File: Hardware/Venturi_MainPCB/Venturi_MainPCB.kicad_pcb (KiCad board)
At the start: 2 copper layers, 166.1 x 84.5 mm, 75 parts, among them J1 Battery, J2 ESC_PWM, J3 ESC_P, J4 ESC_N, J5 M1, J6 M1, J7 Sensor-PCB, Q1 BSS138, Q2 DMP3013SFV, U1 TSOP38238, U2 ESP32-P4-WIFI6, U3 MIC29152WU, U4 DRV8212P, U5 DRV8212P, U6 ICM-20948

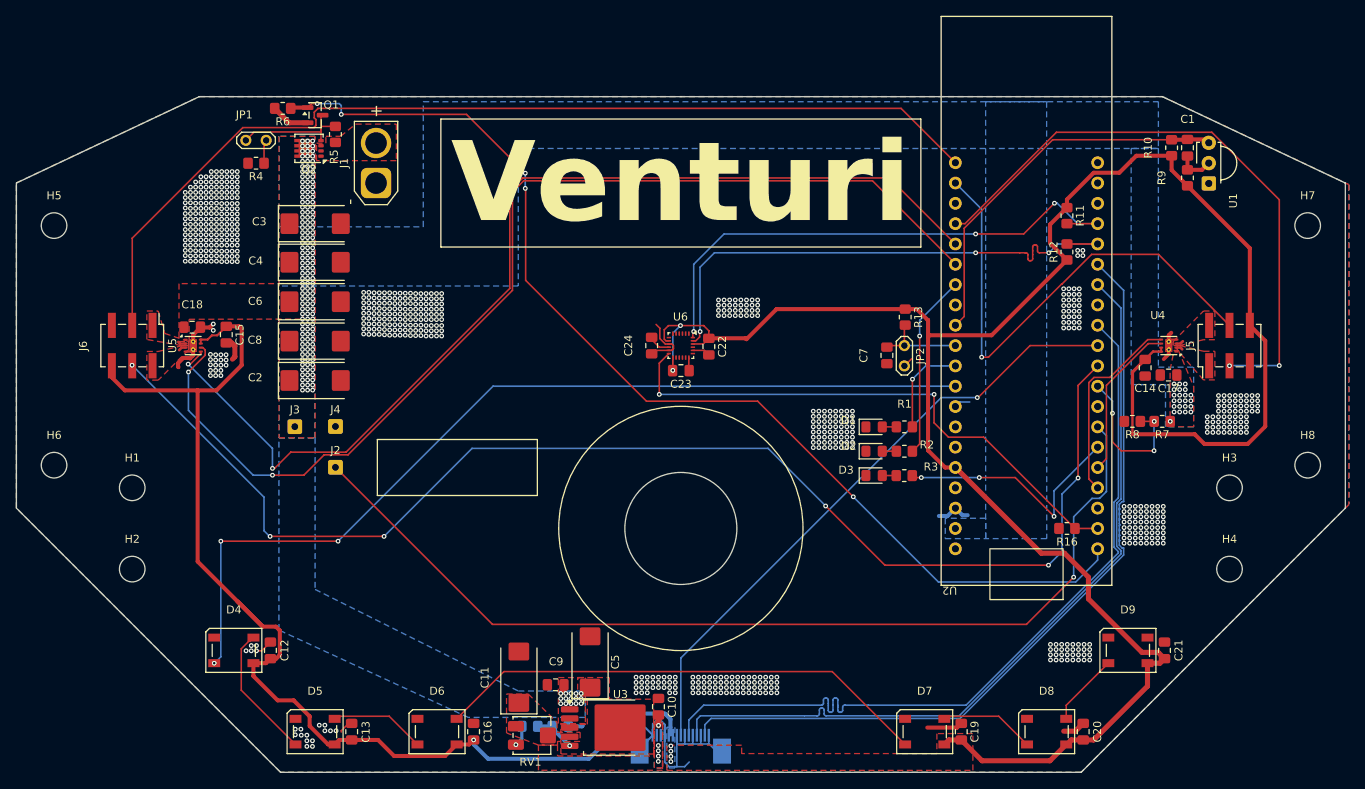
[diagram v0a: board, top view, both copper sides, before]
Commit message: Updated PCB-Design for 20MHz SPI speed
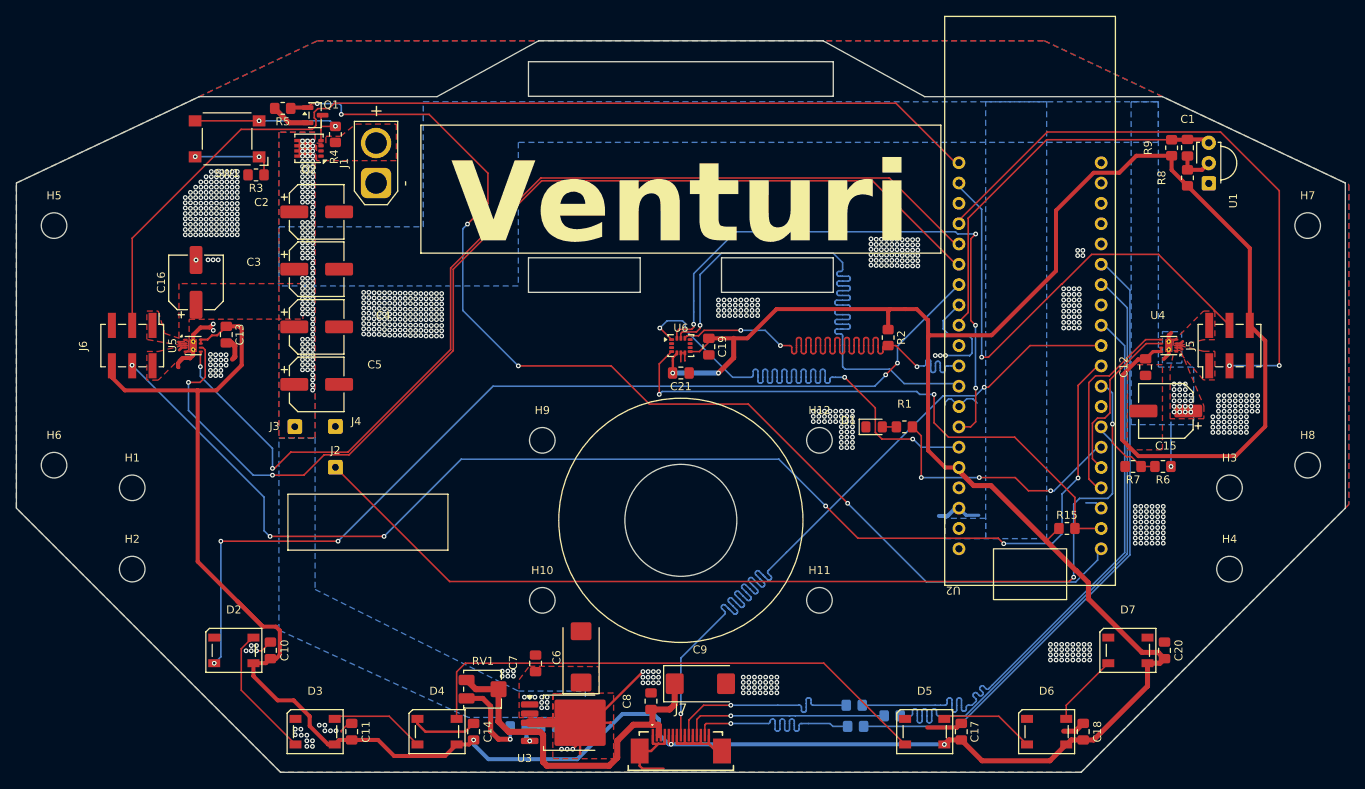
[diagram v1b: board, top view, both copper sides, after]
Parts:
- removed the C17 at (198.8, 93.0)
- removed the C18 at (76.8, 87.0)
- removed C24: 100n, Capacitor_SMD:C_0805_2012Metric_Pad1.18x1.45mm_HandSolder
- removed the C6 at (92.1, 83.8)
- removed the C7 at (163.6, 90.5)
- removed the C8 at (92.1, 88.7)
- removed the D2 at (162.0, 102.5)
- removed the D3 at (162.0, 105.5)
- removed JP1: POWER_EN, TestPoint:TestPoint_2Pads_Pitch2.54mm_Drill0.8mm
- removed JP2: ESP_EN, TestPoint:TestPoint_2Pads_Pitch2.54mm_Drill0.8mm
- removed the R13 at (165.9, 85.7)
- removed the R2 at (165.8, 102.5)
- removed the R3 at (165.8, 105.5)
- added C15: 220uF, Capacitor_SMD:CP_Elec_6.3x9.9, F.Cu at (198.5, 97.5)
- added C16: 220uF, Capacitor_SMD:CP_Elec_6.3x9.9, F.Cu at (77.2, 81.4)
- added C5: 220uF, Capacitor_SMD:CP_Elec_6.3x9.9, F.Cu at (92.3, 94.1)
- added H10: ~, MountingHole:MountingHole_3.2mm_M3_DIN965, F.Cu at (120.5, 121.1)
- added H11: ~, MountingHole:MountingHole_3.2mm_M3_DIN965, F.Cu at (155.2, 121.1)
- added H12: ~, MountingHole:MountingHole_3.2mm_M3_DIN965, F.Cu at (155.2, 101.1)
- added H9: ~, MountingHole:MountingHole_3.2mm_M3_DIN965, F.Cu at (120.5, 101.1)
- added R10: 22R, Resistor_SMD:R_0805_2012Metric_Pad1.20x1.40mm_HandSolder, B.Cu at (159.7, 136.9)
- added R11: 22R, Resistor_SMD:R_0805_2012Metric_Pad1.20x1.40mm_HandSolder, B.Cu at (164.3, 135.6)
- added SW1: POWER_EN, Button_Switch_SMD:SW_SPST_Omron_B3FS-100xP, F.Cu at (81.1, 63.4)
- C2, C3, C4: value 100uF -> 220uF; footprint Capacitor_Tantalum_SMD:CP_EIA-7343-15_Kemet-W_HandSolder -> Capacitor_SMD:CP_Elec_6.3x9.9
- J7: moved to F.Cu
- R12: value 3k3 -> 22R; moved to B.Cu
- U6: value ICM-20948 -> ICM-42670-P; footprint Sensor_Motion:InvenSense_QFN-24_3x3mm_P0.4mm -> Package_LGA:LGA-14_3x2.5mm_P0.5mm_LayoutBorder3x4y
- moved R12 62.6 mm to (159.5, 134.2), turned to 180 degrees
- moved R2 27.1 mm to (163.8, 88.3)
- moved C9 22.7 mm to (140.3, 131.5), turned to 0 degrees
- moved C2 21.1 mm to (92.3, 72.6)
- moved RV1 8.46 mm to (113.1, 132.2)
- moved C4 8.08 mm to (92.3, 86.9)
- moved C3 5.69 mm to (92.3, 79.7)
- moved R6 5.64 mm to (198.1, 104.4)
- moved R7 5.64 mm to (194.4, 104.4)
- moved U3 5.04 mm to (124.0, 136.4)
- moved C7 3.67 mm to (119.7, 129.0), turned to 90 degrees
- moved R3 1.46 mm to (84.7, 67.9)
- moved R14 1.45 mm to (121.3, 136.9)
- moved R13 1.45 mm to (117.5, 136.9)
- moved C6 1.29 mm to (125.4, 128.2)
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- renumbered C12 to C10, C13 to C11, C14 to C12, C15 to C13, C16 to C14, C19 to C17, C20 to C18, C22 to C19, C21 to C20, C23 to C21, C5 to C6, C9 to C7, C10 to C8, C11 to C9, D4 to D2, D5 to D3, D6 to D4, D7 to D5, D8 to D6, D9 to D7, R14 to R13, R15 to R14, R16 to R15, R11 to R2, R4 to R3, R5 to R4, R6 to R5, R7 to R6, R8 to R7, R9 to R8, R10 to R9
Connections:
- J7 pad 10: +3V3 -> MOSI
- J7 pad 11: +3V3 -> GND
- J7 pad 12: GND -> CLK
- J7 pad 13: VCC -> GND
- J7 pad 14: VCC -> CS
- J7 pad 2: CS -> VCC
- J7 pad 3: GND -> VCC
- J7 pad 4: CLK -> GND
- J7 pad 5: GND -> +3V3
- J7 pad 6: MOSI -> +3V3
- R1 pad 1: Net-(U2-GPIO23) -> Net-(U2-GPIO29)
- R12 pad 1: +3V3 -> Net-(U2-GPIO4)
- R12 pad 2: IMU_SCL -> MOSI
- R15 pad 1: IMU_INT -> +3V3
- R15 pad 2: GND -> IMU_INT
- R2 pad 2: IMU_SDA -> IMU_CS
- U2 pad 11: IMU_SDA -> unconnected-(U2-GPIO7-Pad11)
- U2 pad 12: IMU_SCL -> unconnected-(U2-GPIO8-Pad12)
- U2 pad 13: unconnected-(U2-GPIO20-Pad13) -> IMU_MISO
- U2 pad 14: unconnected-(U2-GPIO21-Pad14) -> IMU_MOSI
- U2 pad 15: SK6812 -> IMU_CLK
- U2 pad 16: Net-(U2-GPIO23) -> IMU_CS
- U2 pad 18: Net-(U2-GPIO27) -> SK6812
- U2 pad 5: Net-(JP2-A) -> unconnected-(U2-ESP_EN-Pad5)
- U2 pad 7: CS -> Net-(U2-GPIO2)
- U2 pad 8: CLK -> Net-(U2-GPIO3)
- U2 pad 9: MOSI -> Net-(U2-GPIO4)
- U6 pad 1: unconnected-(U6-NC-Pad1) -> IMU_MISO
- U6 pad 10: Net-(U6-REGOUT) -> unconnected-(U6-RESV-Pad10)
- U6 pad 11: GND -> unconnected-(U6-RESV-Pad11)
- U6 pad 12: IMU_INT -> IMU_CS
- U6 pad 13: +3V3 -> IMU_CLK
- U6 pad 14: unconnected-(U6-NC-Pad14) -> IMU_MOSI
- U6 pad 4: unconnected-(U6-NC-Pad4) -> IMU_INT
- U6 pad 5: unconnected-(U6-NC-Pad5) -> +3V3
- U6 pad 6: unconnected-(U6-NC-Pad6) -> GND
- U6 pad 7: unconnected-(U6-AUX_CL-Pad7) -> GND
- U6 pad 9: GND -> unconnected-(U6-INT2-Pad9)
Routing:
- net Net-(U2-GPIO2): track 0.00 -> 79.8 mm
- net Net-(U2-GPIO4): track 0.00 -> 78.9 mm
- net Net-(U2-GPIO3): track 0.00 -> 78.9 mm
- net IMU_CLK: track 0.00 -> 78.2 mm, vias 0 -> 1
- net MOSI: track 100.4 -> 25.3 mm, vias 0 -> 1
- net IMU_CS: track 0.00 -> 75.0 mm, vias 0 -> 3
- net CLK: track 100.4 -> 25.6 mm, vias 0 -> 1
- net CS: track 101.2 -> 26.5 mm, vias 0 -> 1
- net IMU_MOSI: track 0.00 -> 73.8 mm, vias 0 -> 4
- net IMU_MISO: track 0.00 -> 72.3 mm, vias 0 -> 3
- net IMU_SCL: track 67.8 -> 0.00 mm, vias 3 -> 0
- net IMU_SDA: track 67.8 -> 0.00 mm, vias 3 -> 0
- net GND: track 85.7 -> 132.1 mm, vias 755 -> 674
- net VCC: track 1.30 -> 45.8 mm, vias 5 -> 0
- net +3V3: track 405.2 -> 447.1 mm, vias 7 -> 5
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- removed copper zone on B.Cu, net +3V3
- removed copper zone on F.Cu, net +3V3
- removed copper zone on B.Cu, net VCC
- removed copper zone on F.Cu, net VCC
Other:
- board size 166.1 x 84.5 mm -> 166.1 x 91.4 mm
